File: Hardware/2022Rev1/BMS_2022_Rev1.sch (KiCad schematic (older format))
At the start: 104 parts, among them Q1 2N7000, Q2 IRFS7530, Q3 2N7000, Q4 IRFS7530, SW1 Relay_SPST, U1 LT1910, U10 AD8278BRZ, U11 AD8278BRZ, U12 AD8278BRZ, U13 AD8278BRZ, U2 TM4C129E_Launchpad, U3 OKI, U4 OKI, U5 ACS759ECB-200B-PFF-T, U6 OKI, U7 AD8278BRZ, U8 AD8278BRZ, U9 AD8278BRZ

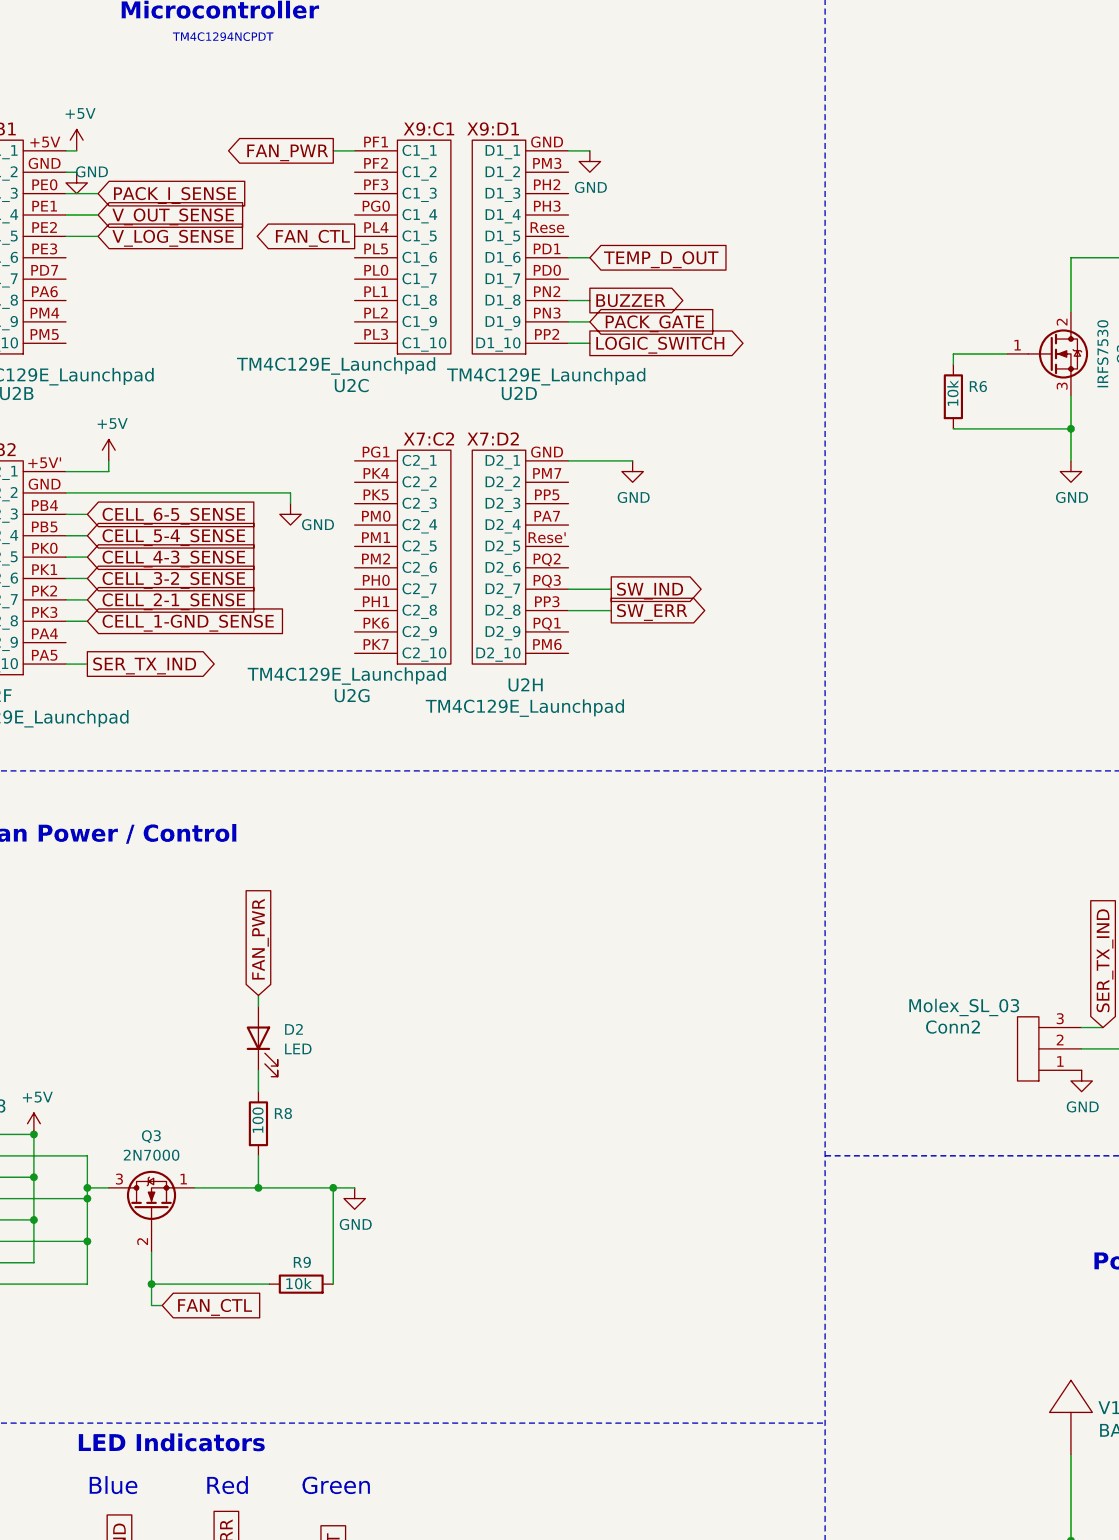
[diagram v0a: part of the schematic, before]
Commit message: consistency check
added missing tag, wires
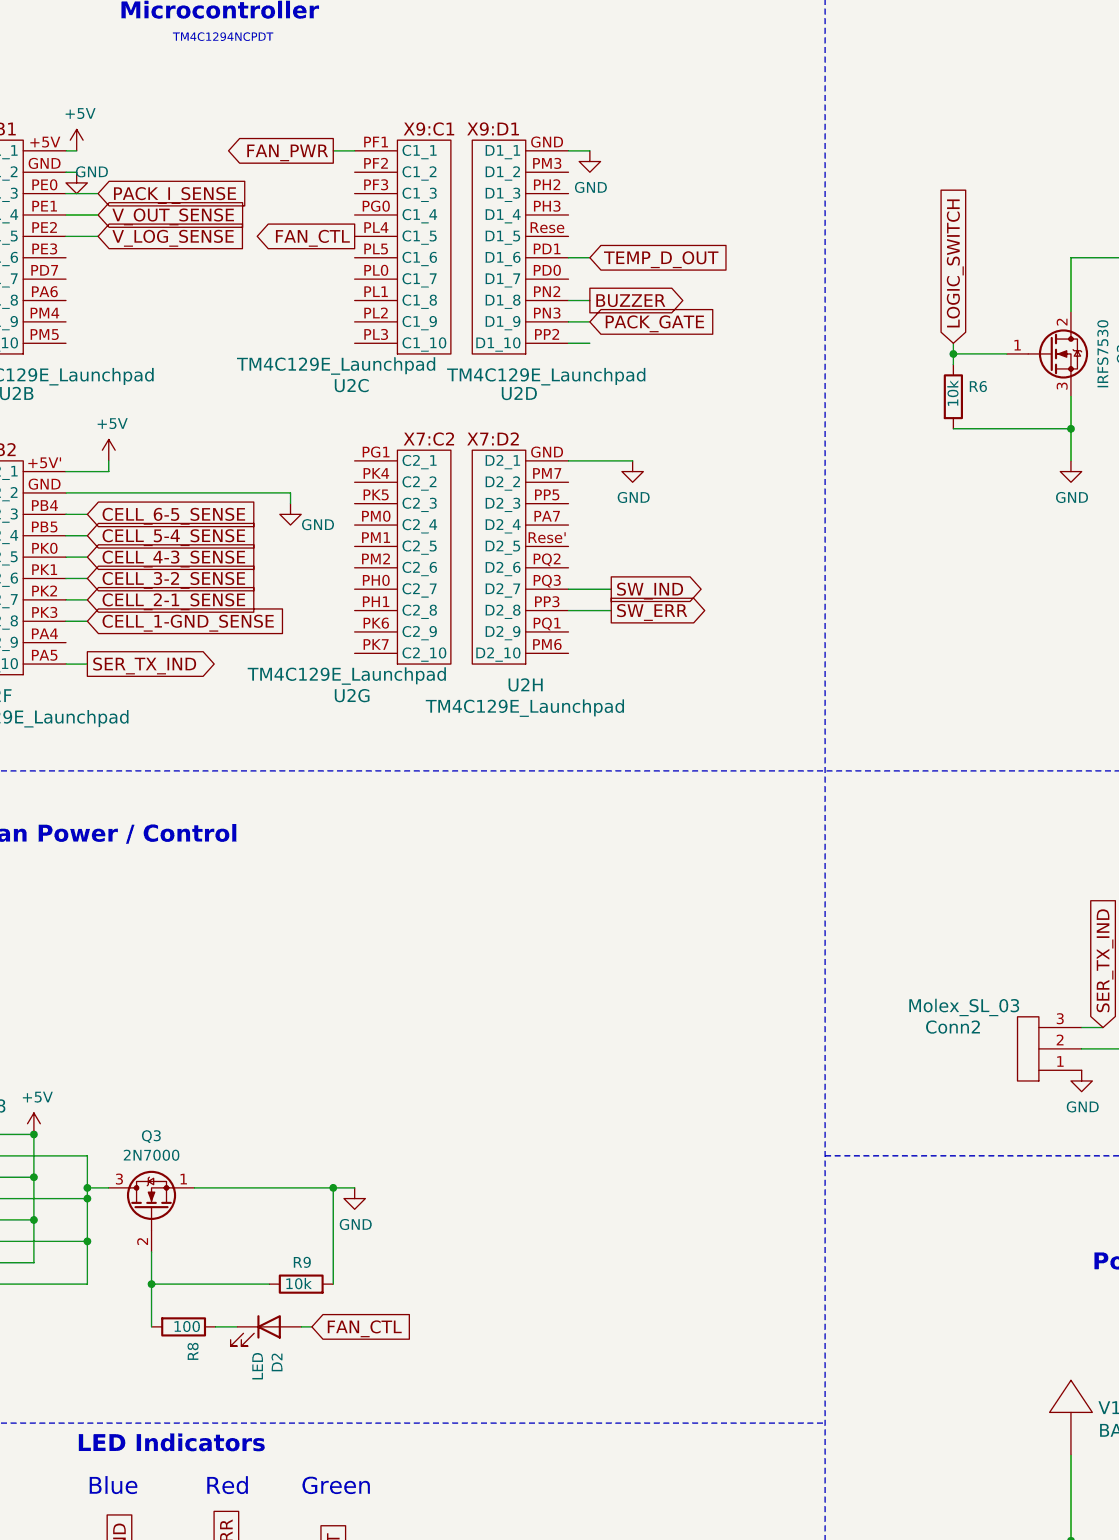
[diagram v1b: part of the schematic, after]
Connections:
- wire segments 351 -> 349
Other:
- moved on the sheet: D2, R8
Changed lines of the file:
@@
 	1    0    0    -1
 $EndComp
-Wire Wire Line
-	3200 6150 3500 6150
 Connection ~ 3850 6150
 Wire Wire Line
@@
 $EndComp
 Wire Wire Line
-	3500 6150 3500 6000
-Wire Wire Line
-	3500 5700 3500 5600
+	3300 6800 3400 6800
 $Comp
 L Device:R R8
 U 1 1 616059CC
-P 3500 5850
-F 0 "R8" H 3570 5896 50  0000 L CNN
-F 1 "100" V 3500 5800 50  0000 L CNN
-F 2 "" V 3430 5850 50  0001 C CNN
-F 3 "~" H 3500 5850 50  0001 C CNN
-	1    3500 5850
-	1    0    0    -1
-$EndComp
-Wire Wire Line
-	3500 5300 3500 5250
+P 3150 6800
+F 0 "R8" H 3220 6846 50  0000 L CNN
+F 1 "100" V 3150 6750 50  0000 L CNN
+F 2 "" V 3080 6800 50  0001 C CNN
+F 3 "~" H 3150 6800 50  0001 C CNN
+	1    3150 6800
+	0    1    1    0
+$EndComp
+Wire Wire Line
+	3700 6800 3750 6800
 Wire Wire Line
 	3850 8150 3850 8100
@@
 	3000 6450 3000 6600
 Wire Wire Line
-	3000 6700 3050 6700
-Wire Wire Line
 	3550 6600 3000 6600
 Connection ~ 3000 6600
-Wire Wire Line
-	3000 6600 3000 6700
 Wire Wire Line
 	2200 6100 2450 6100
@@
 Text GLabel 19650 2400 0    59   Input ~ 0
 BUZZER
-Text GLabel 3050 6700 2    59   Input ~ 0
+Text GLabel 3750 6800 2    59   Input ~ 0
 FAN_CTL
 Text GLabel 7450 5400 1    59   Input ~ 0
@@
 Text GLabel 3850 8100 1    59   Input ~ 0
 V_OUT
-Text GLabel 3500 5250 1    59   Input ~ 0
-FAN_PWR
 Wire Wire Line
 	2600 1400 2650 1400
@@
 Text GLabel 5050 2100 2    59   Input ~ 0
 PACK_GATE
-Text GLabel 5050 2200 2    59   Output ~ 0
+Text GLabel 6750 2200 1    59   Input ~ 0
 LOGIC_SWITCH
 Wire Wire Line
@@
 	1    0    0    -1
 $EndComp
-Connection ~ 3500 6150
-Wire Wire Line
-	3500 6150 3850 6150
 $Comp
 L Device:LED D7
@@
 L Device:LED D2
 U 1 1 61C99EFA
-P 3500 5450
-F 0 "D2" V 3539 5332 50  0000 R CNN
-F 1 "LED" V 3448 5332 50  0000 R CNN
-F 2 "" H 3500 5450 50  0001 C CNN
-F 3 "~" H 3500 5450 50  0001 C CNN
-	1    3500 5450
-	0    -1   -1   0
+P 3550 6800
+F 0 "D2" V 3589 6682 50  0000 R CNN
+F 1 "LED" V 3498 6682 50  0000 R CNN
+F 2 "" H 3550 6800 50  0001 C CNN
+F 3 "~" H 3550 6800 50  0001 C CNN
+	1    3550 6800
+	1    0    0    -1
 $EndComp
 Wire Notes Line
@@
 	1    0    0    -1
 $EndComp
+Wire Wire Line
+	3000 6600 3000 6800
+Wire Wire Line
+	3200 6150 3850 6150
+Wire Wire Line
+	6750 2250 6750 2200
+Connection ~ 6750 2250
 $EndSCHEMATC

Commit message: Changed the 9V battery Circuit to 3 terminal switch
Changed the 9V battery to a 3 terminal switch to change from the 9v battery power to the battery pack power or off at any given switch change
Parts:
- removed BT1: 9V, symbol Device:Battery
- added 9V1: Battery, symbol Device:Battery
- added D?: 3.3V, symbol Device:D_Zener
- added D?: 4.3V, symbol Device:D_Zener
- added R? (x2): 10k, symbol Device:R
- added R? (x2): 1.5k, symbol Device:R
- added SW2: SW_SP3T, symbol Switch:SW_SP3T
- added U?: AD8278BRZ, SOIC127P600X175-8N, symbol BMS_2022_Rev1-rescue:AD8278BRZ-BMS_2022
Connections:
- net labels added: 3_WAY_SW_V, CELL_1_GND_SENSE, PV
- net labels removed: +9V, CELL_1-GND_SENSE, CELL_2-1_SENSE, CELL_3-2_SENSE, CELL_4-3_SENSE, CELL_5-4_SENSE, CELL_6-5_SENSE, CELL_7-6_SENSE, CELL_8-7_SENSE, I_MEAS_OUT
- wire segments 349 -> 389
- no-connect marks 2 -> 3
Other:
- note added: "3 WAY SWITCH"
- note added: "TIVA/CELL FILTER POWER"
- note removed: "9V Battery"
- note removed: "TIVA/CELL FITLER POWER"
- moved on the sheet: D10, D11, D12, D13, D14, D15, D16, D17, D18, D19, D20, D21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

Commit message: Fixed labels
changed the directions of the labels to properly be organized for ladybug debugger
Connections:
- wire segments 389 -> 401
- no-connect marks 3 -> 57
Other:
- moved on the sheet: 9V1, BZ1, C1, Conn1, Conn2, Conn3, D1, D10, D11, D12, D13, D14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

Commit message: Organized the power output part of circuit
organized power output part of circuit to make circuit logically flow
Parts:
- removed C10: 1uF, symbol Device:C
- removed C8: 22uF, symbol Device:CP1
- removed C9: 10uF, symbol Device:C
- removed U6: OKI, symbol MRDT_Devices:OKI
- gave numbers to parts that had none: 7
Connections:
- net labels removed: 3_WAY_SW_V, V_IN
- wire segments 401 -> 387
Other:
- note removed: "TIVA/CELL FILTER POWER"
- moved on the sheet: 9V1, C1, C2, C3, C4, C5, C6, C7, Conn1, Conn2, Conn4A, Conn4B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

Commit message: Replaced Differential Op-Amp because of Chip Shortage
Replace Differential Op-Amp because of chip shortage and replaced the schematic layout of Cell Monitor with the Generic Differential Op-Amp layout with matching resistor and diode values of the Differential Op-Amp ordered
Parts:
- removed D10, D11, D12, D13, D14, D22, D8, D9: 3.3V, symbol Device:D_Zener
- removed D15, D16, D17, D18, D19, D20, D21, D23: 4.3V, symbol Device:D_Zener
- removed R17, R19, R21, R22, R23, R24, R25, R31, R32, R33, R34, R35, R36, R43, R45: 1.5k, symbol Device:R
- removed R18, R20, R26, R27, R28, R29, R30, R37, R38, R39, R40, R41, R42, R44, R46: 10k, symbol Device:R
- removed U10, U11, U12, U13, U6, U7, U8, U9: AD8278BRZ, SOIC127P600X175-8N, symbol BMS_2022_Rev1-rescue:AD8278BRZ-BMS_2022
- added D? (x8): 4.3V, symbol Device:D_Zener
- added D? (x8): 3.3V, symbol Device:D_Zener
- added R? (x16): 40k, symbol Device:R
- added R? (x16): 31.5k, symbol Device:R
- added U? (x12): Opamp_Dual_Generic, symbol Device:Opamp_Dual_Generic
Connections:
- net CELL_1_GND_SENSE: now also D?.1 (K), R?.1, U?.1
- net CELL_2_1_SENSE: now also D?.1 (K), R?.1, U?.7
- net CELL_3_2_SENSE: now also D?.1 (K), R?.1, U?.1
- net CELL_4_3_SENSE: now also D?.1 (K), R?.1, U?.7
- net CELL_5_4_SENSE: now also D?.1 (K), R?.1, U?.1
- net CELL_6_5_SENSE: now also D?.1 (K), R?.1, U?.7
- net CELL_7_6_SENSE: now also D?.1 (K), R?.1, U?.1
- net CELL_8_7_SENSE: now also D?.1 (K), R?.1, U?.7
- net GND: now also D?.2 (A), D?.2 (A), D?.2 (A), D?.2 (A), D?.2 (A), D?.2 (A), D?.2 (A), D?.2 (A), D?.2 (A), R?.1, R?.1, R?.1, R?.1, R?.1, R?.1, R?.1, R?.1, R?.2, U?.4 (V-), U?.4 (V-), U?.4 (V-), U?.4 (V-)
- net PACK_V: now reaches C1.1, Q4.2 (D), SW2.1, U1.6 (SENSE), U1.8 (V+), U5.5 (IP-)
- net PACK_V: now also U?.8 (V+), U?.8 (V+), U?.8 (V+), U?.8 (V+)
- new net: R?.1, R?.2, U?.2 (-) (x4)
- new net: R?.1, R?.2, U?.3 (+) (x4)
- new net: D?.1 (K), D?.2 (A), R?.2, R?.2 (x7)
- new net: R?.1, R?.2, U?.5 (+) (x4)
- new net: R?.1, R?.2, U?.6 (-) (x4)
- new net: D?.1 (K), R?.2
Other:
- note added: "Cell 1"
- note added: "Cell 2"
- note added: "Cell 3"
- note added: "Cell 4"
- note added: "Cell 5"
- note added: "Cell 6"
- note added: "Cell 7"
- note added: "Cell 8"
- note added: "Cell Monitor"
- note removed: "Cell Filter"
- moved on the sheet: BZ1, Conn2, Conn6, Conn7, Q1, R5

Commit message: Deleted BMS Logic Switch and fixed: no connects, flags, and cell voltage monitor connections
Completed Troubleshooting for Ladybug by simplifying BMS schematic. Deleted BMS Logic Switch since we have 3 way switch. Fixed flags and no connect issues for Ladybug problem analysis
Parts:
- removed D1: 3.3V, symbol Device:D_Zener
- removed Q2: IRFS7530, symbol Device:Q_NMOS_GDS
- removed R3: 1M, symbol Device:R
- removed R6: 10k, symbol Device:R
- removed R7: 100k, symbol Device:R
- removed SW1: Relay_SPST, symbol BMS_2022_Rev1-rescue:Relay_SPST-MRDT_Switches-BMS_2022_Rev1-rescue
- gave numbers to parts that had none: 52
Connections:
- net LOG_PWR is gone; now on net PACK_V: F1.1
- net CELL_1: now also D20.2 (A), D22.1 (K), R43.2, R46.2
- net CELL_2: now also D18.2 (A), D20.1 (K), R39.2, R42.2
- net CELL_3: now also D16.2 (A), D18.1 (K), R35.2, R38.2
- net CELL_4: now also D14.2 (A), D16.1 (K), R31.2, R34.2
- net CELL_5: now also D12.2 (A), D14.1 (K), R27.2, R30.2
- net CELL_6: now also D10.2 (A), D12.1 (K), R23.2, R26.2
- net CELL_7: now also D10.1 (K), D8.2 (A), R19.2, R22.2
- net CELL_8: now also D8.1 (K), R18.2
- net PACK_V: no longer U5.5 (IP-)
- net at F1.2: now also U5.5 (IP-)
- net FAN_PWR: no longer names the net of U2.PF1 (C1_1)
- net V_LOG_SENSE: no longer names the net of U2.PE2 (B1_5)
- no-connect marks 57 -> 60
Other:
- note removed: "BMS Logic Switch"
- moved on the sheet: Conn4A, Conn4B, F1, U5, V1, V2

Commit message: Replaced SL Molex connectors with Microfit Molex connectors
Replaced SL Molex connectors with Micro fit Molex connectors because Micro fit is more structurally sound
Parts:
- removed Conn1: E-Stop-LED, symbol BMS_2022_Rev1-rescue:Molex_SL_04-MRDT_Connectors-BMS_2022_Rev1-rescue
- removed Conn2: Molex_SL_03, symbol BMS_2022_Rev1-rescue:Molex_SL_03-MRDT_Connectors-BMS_2022_Rev1-rescue
- removed Conn3: Molex_SL_08, symbol MRDT_Connectors:Molex_SL_08
- removed Conn5: TEMP_SENS, symbol BMS_2022_Rev1-rescue:Molex_SL_03-MRDT_Connectors-BMS_2022_Rev1-rescue
- added Conn?: Molex_SL_08, symbol MRDT_Connectors:Molex_SL_08
- added J? (x2): Molex_uF_SV_03, MRDT_Connectors:MOLEX_uF_S_03_Vertical, symbol MRDT_Connectors:Molex_uF_SV_03
- added J?: Molex_uF_SV_04, MRDT_Connectors:MOLEX_uF_S_04_Vertical, symbol MRDT_Connectors:Molex_uF_SV_04
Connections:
- net +3V3: now also J?.2, J?.3
- net +5V: now also Conn?.2, Conn?.4, Conn?.6, Conn?.8
- net GND: now also J?.1, J?.1, J?.4
- net PACK_GATE: now also J?.2
- net SER_TX_IND: now also J?.3
- net TEMP_D_OUT: now also J?.2
- net at Q3.3 (D): now also Conn?.1, Conn?.3, Conn?.5, Conn?.7
- net at R1.1, U1.4 (IN): now also J?.1
- net at R2.1, R4.1: now also J?.3
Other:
- moved on the sheet: 9V1, BZ1, C1, C2, C3, C4, C5, C6, C7, Conn4A, Conn4B, D3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

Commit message: Started generating the PCB Footprint Layout
Started the PCB footprint layout, but I am updating the libraries
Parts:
- BZ1: footprint (none) -> MRDT_Devices:BUZZER_SMI_1324_TW_5V_2_R
- C1, C2, C3, C4, C5, C6, C7: footprint (none) -> Capacitor_SMD:C_0603_1608Metric_Pad1.08x0.95mm_HandSolder
- D2: footprint (none) -> LED_SMD:LED_0603_1608Metric_Pad1.05x0.95mm_HandSolder
- D3: footprint (none) -> Diode_SMD:D_0603_1608Metric_Pad1.05x0.95mm_HandSolder
- gave numbers to parts that had none: 4
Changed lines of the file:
@@
 F 0 "C1" H 15065 2746 50  0000 L CNN
 F 1 "10u" H 15065 2655 50  0000 L CNN
-F 2 "" H 14988 2550 50  0001 C CNN
+F 2 "Capacitor_SMD:C_0603_1608Metric_Pad1.08x0.95mm_HandSolder" H 14988 2550 50  0001 C CNN
 F 3 "~" H 14950 2700 50  0001 C CNN
 	1    14950 2700
@@
 F 0 "BZ1" H 13405 6975 50  0000 C CNN
 F 1 "Buzzer" H 13405 7066 50  0000 C CNN
-F 2 "" V 13375 7400 50  0001 C CNN
+F 2 "MRDT_Devices:BUZZER_SMI_1324_TW_5V_2_R" V 13375 7400 50  0001 C CNN
 F 3 "~" V 13375 7400 50  0001 C CNN
 	1    13400 7300
@@
 F 0 "C5" H 12615 4946 50  0000 L CNN
 F 1 "22uF" H 12615 4855 50  0000 L CNN
-F 2 "" H 12500 4900 50  0001 C CNN
+F 2 "Capacitor_SMD:C_0603_1608Metric_Pad1.08x0.95mm_HandSolder" H 12500 4900 50  0001 C CNN
 F 3 "~" H 12500 4900 50  0001 C CNN
 	1    12500 4900
@@
 F 0 "C6" H 14515 4946 50  0000 L CNN
 F 1 "10uF" H 14515 4855 50  0000 L CNN
-F 2 "" H 14438 4750 50  0001 C CNN
+F 2 "Capacitor_SMD:C_0603_1608Metric_Pad1.08x0.95mm_HandSolder" H 14438 4750 50  0001 C CNN
 F 3 "~" H 14400 4900 50  0001 C CNN
 	1    14400 4900
@@
 F 0 "C7" H 14965 4946 50  0000 L CNN
 F 1 "1uF" H 14965 4855 50  0000 L CNN
-F 2 "" H 14888 4750 50  0001 C CNN
+F 2 "Capacitor_SMD:C_0603_1608Metric_Pad1.08x0.95mm_HandSolder" H 14888 4750 50  0001 C CNN
 F 3 "~" H 14850 4900 50  0001 C CNN
 	1    14850 4900
@@
 F 0 "C2" H 16515 4996 50  0000 L CNN
 F 1 "22uF" H 16515 4905 50  0000 L CNN
-F 2 "" H 16400 4950 50  0001 C CNN
+F 2 "Capacitor_SMD:C_0603_1608Metric_Pad1.08x0.95mm_HandSolder" H 16400 4950 50  0001 C CNN
 F 3 "~" H 16400 4950 50  0001 C CNN
 	1    16400 4950
@@
 F 0 "C3" H 18715 4996 50  0000 L CNN
 F 1 "10uF" H 18715 4905 50  0000 L CNN
-F 2 "" H 18638 4800 50  0001 C CNN
+F 2 "Capacitor_SMD:C_0603_1608Metric_Pad1.08x0.95mm_HandSolder" H 18638 4800 50  0001 C CNN
 F 3 "~" H 18600 4950 50  0001 C CNN
 	1    18600 4950
@@
 F 0 "C4" H 19165 4996 50  0000 L CNN
 F 1 "1uF" H 19165 4905 50  0000 L CNN
-F 2 "" H 19088 4800 50  0001 C CNN
+F 2 "Capacitor_SMD:C_0603_1608Metric_Pad1.08x0.95mm_HandSolder" H 19088 4800 50  0001 C CNN
 F 3 "~" H 19050 4950 50  0001 C CNN
 	1    19050 4950
@@
 F 0 "D2" V 3539 6132 50  0000 R CNN
 F 1 "LED" V 3448 6132 50  0000 R CNN
-F 2 "" H 3500 6250 50  0001 C CNN
+F 2 "LED_SMD:LED_0603_1608Metric_Pad1.05x0.95mm_HandSolder" H 3500 6250 50  0001 C CNN
 F 3 "~" H 3500 6250 50  0001 C CNN
 	1    3500 6250
@@
 F 0 "D3" H 12850 2683 50  0000 C CNN
 F 1 "3.3V" H 12850 2774 50  0000 C CNN
-F 2 "" H 12850 2900 50  0001 C CNN
+F 2 "Diode_SMD:D_0603_1608Metric_Pad1.05x0.95mm_HandSolder" H 12850 2900 50  0001 C CNN
 F 3 "~" H 12850 2900 50  0001 C CNN
 	1    12850 2900
@@
 	10600 15200 11250 15200
 $Comp
-L MRDT_Connectors:Molex_uF_SV_03 J?
+L MRDT_Connectors:Molex_uF_SV_03 J1
 U 1 1 62335026
 P 2650 10100
-F 0 "J?" H 2593 9833 50  0000 C CNN
+F 0 "J1" H 2593 9833 50  0000 C CNN
 F 1 "Molex_uF_SV_03" H 2593 9924 50  0000 C CNN
 F 2 "MRDT_Connectors:MOLEX_uF_S_03_Vertical" H 2650 10100 50  0001 L BNN
@@
 $EndComp
 $Comp
-L MRDT_Connectors:Molex_uF_SV_03 J?
+L MRDT_Connectors:Molex_uF_SV_03 J2
 U 1 1 62365ECD
 P 18600 9900
-F 0 "J?" H 18750 9650 50  0000 C CNN
+F 0 "J2" H 18750 9650 50  0000 C CNN
 F 1 "Molex_uF_SV_03" H 18750 9750 50  0000 C CNN
 F 2 "MRDT_Connectors:MOLEX_uF_S_03_Vertical" H 18600 9900 50  0001 L BNN
@@
 	18800 10150 18800 10100
 $Comp
-L MRDT_Connectors:Molex_uF_SV_04 J?
+L MRDT_Connectors:Molex_uF_SV_04 J3
 U 1 1 6239943E
 P 19200 2000
-F 0 "J?" V 19189 1770 50  0000 R CNN
+F 0 "J3" V 19189 1770 50  0000 R CNN
 F 1 "Molex_uF_SV_04" V 19098 1770 50  0000 R CNN
 F 2 "MRDT_Connectors:MOLEX_uF_S_04_Vertical" H 19200 2000 50  0001 L BNN
@@
 $EndComp
 $Comp
-L MRDT_Connectors:Molex_SL_08 Conn?
+L MRDT_Connectors:Molex_SL_08 Conn1
 U 1 1 623C06A0
 P 1950 5300
-F 0 "Conn?" H 1892 5113 60  0000 C CNN
+F 0 "Conn1" H 1892 5113 60  0000 C CNN
 F 1 "Molex_SL_08" H 1892 5219 60  0000 C CNN
 F 2 "" H 1950 5600 60  0001 C CNN
